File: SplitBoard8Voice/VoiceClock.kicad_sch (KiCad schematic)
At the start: 41 parts, among them U1001 74HC74, U1002 74HC595, U1003 74HC74, U1004 74HC08, U1005 74HC595, U1006 74HC14, U1007 74HC14

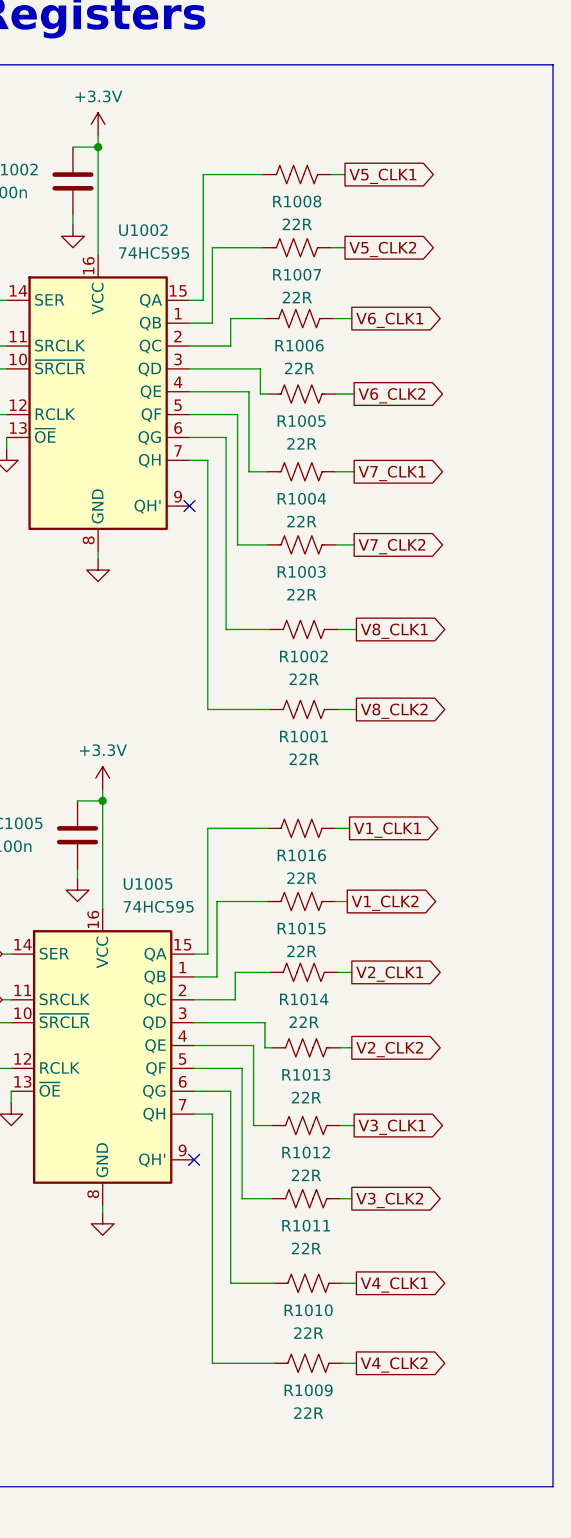
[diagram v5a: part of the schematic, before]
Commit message: some 8voice routing
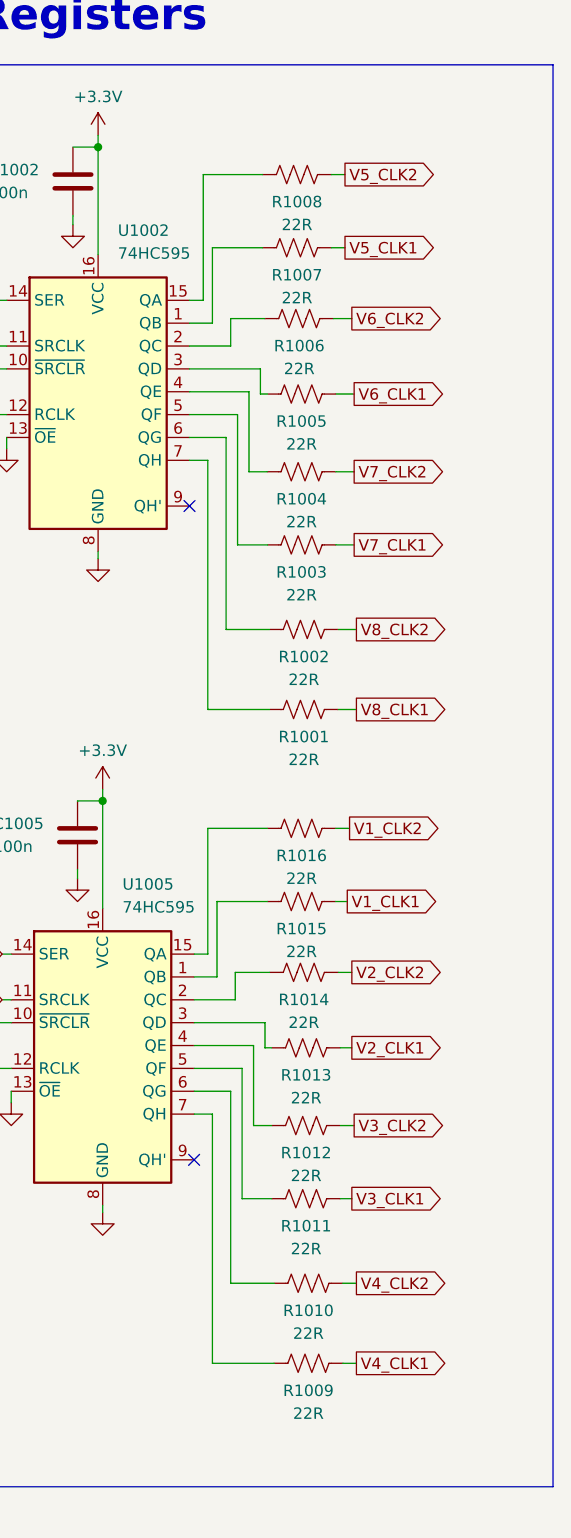
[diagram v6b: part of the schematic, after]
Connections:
- net V1_CLK1: now also R1015.2; no longer R1016.2
- net V1_CLK2: now also R1016.2; no longer R1015.2
- net V2_CLK1: now also R1013.2; no longer R1014.2
- net V2_CLK2: now also R1014.2; no longer R1013.2
- net V3_CLK1: now also R1011.2; no longer R1012.2
- net V3_CLK2: now also R1012.2; no longer R1011.2
- net V4_CLK1: now also R1009.2; no longer R1010.2
- net V4_CLK2: now also R1010.2; no longer R1009.2
- net V5_CLK1: now also R1007.2; no longer R1008.2
- net V5_CLK2: now also R1008.2; no longer R1007.2
- net V6_CLK1: now also R1005.2; no longer R1006.2
- net V6_CLK2: now also R1006.2; no longer R1005.2
- net V7_CLK1: now also R1003.2; no longer R1004.2
- net V7_CLK2: now also R1004.2; no longer R1003.2
- net V8_CLK1: now also R1001.2; no longer R1002.2
- net V8_CLK2: now also R1002.2; no longer R1001.2

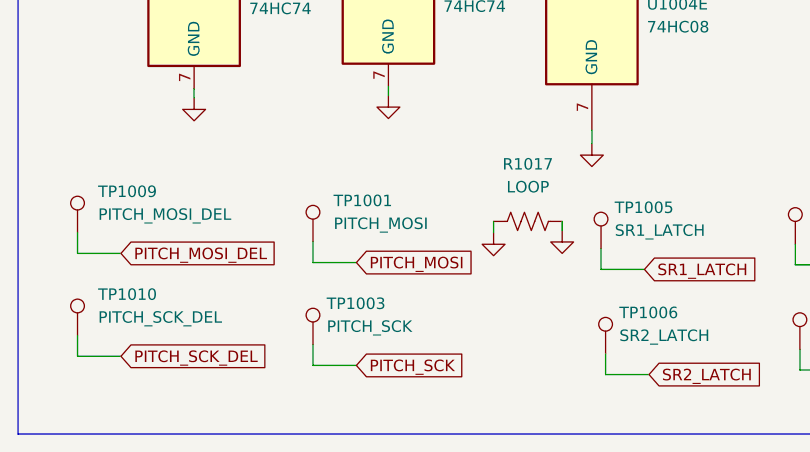
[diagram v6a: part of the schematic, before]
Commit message: transfer vias and test points added
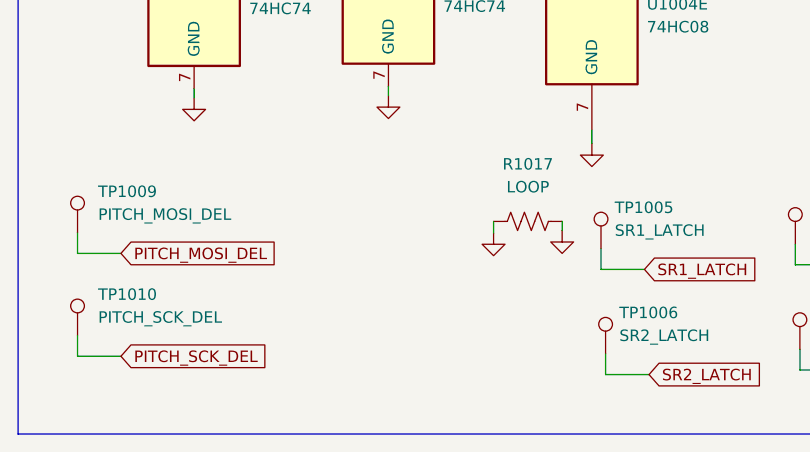
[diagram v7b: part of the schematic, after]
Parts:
- removed TP1001: PITCH_MOSI, TestPoint:TestPoint_THTPad_D1.0mm_Drill0.5mm_VAL, symbol Connector:TestPoint
- removed TP1003: PITCH_SCK, TestPoint:TestPoint_THTPad_D1.0mm_Drill0.5mm_VAL, symbol Connector:TestPoint
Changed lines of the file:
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@@
 	(wire
 		(pts
-			(xy 70.866 238.506) (xy 70.866 240.792)
-		)
-		(stroke
-			(width 0)
-			(type default)
-		)
-	)
-	(wire
-		(pts
 			(xy 336.55 46.99) (xy 338.074 46.99)
 		)
@@
 	(wire
 		(pts
-			(xy 70.866 240.792) (xy 75.692 240.792)
-		)
-		(stroke
-			(width 0)
-			(type default)
-		)
-	)
-	(wire
-		(pts
 			(xy 154.432 59.69) (xy 159.766 59.69)
 		)
@@
 	(wire
 		(pts
-			(xy 70.866 229.362) (xy 75.692 229.362)
-		)
-		(stroke
-			(width 0)
-			(type default)
-		)
-	)
-	(wire
-		(pts
 			(xy 298.958 73.66) (xy 300.482 73.66)
 		)
@@
 	(wire
 		(pts
-			(xy 70.866 227.076) (xy 70.866 229.362)
-		)
-		(stroke
-			(width 0)
-			(type default)
-		)
-	)
-	(wire
-		(pts
 			(xy 157.988 42.672) (xy 179.324 42.672)
 		)
@@
 		)
 	)
-	(global_label "PITCH_SCK"
-		(shape input)
-		(at 75.692 240.792 0)
-		(fields_autoplaced yes)
-		(effects
-			(font
-				(size 1.27 1.27)
-			)
-			(justify left)
-		)
-		(property "Intersheetrefs" "${INTERSHEET_REFS}"
-			(at 88.8372 240.792 0)
-			(effects
-				(font
-					(size 1.27 1.27)
-				)
-				(justify left)
-				(hide yes)
-			)
-		)
-	)
 	(global_label "V6_CLK2"
 		(shape output)
@@
 		)
 	)
-	(global_label "PITCH_MOSI"
-		(shape input)
-		(at 75.692 229.362 0)
-		(fields_autoplaced yes)
-		(effects
-			(font
-				(size 1.27 1.27)
-			)
-			(justify left)
-		)
-		(property "Intersheetrefs" "${INTERSHEET_REFS}"
-			(at 89.6839 229.362 0)
-			(effects
-				(font
-					(size 1.27 1.27)
-				)
-				(justify left)
-				(hide yes)
-			)
-		)
-	)
 	(symbol
 		(lib_id "Connector:TestPoint")
@@
 		(exclude_from_sim no)
 		(in_bom no)
-		(on_board no)
+		(on_board yes)
 		(dnp no)
 		(fields_autoplaced yes)
@@
 		(exclude_from_sim no)
 		(in_bom no)
-		(on_board no)
+		(on_board yes)
 		(dnp no)
 		(fields_autoplaced yes)
@@
 	)
 	(symbol
-		(lib_id "Connector:TestPoint")
-		(at 70.866 227.076 0)
-		(unit 1)
-		(exclude_from_sim no)
-		(in_bom no)
-		(on_board no)
-		(dnp no)
-		(fields_autoplaced yes)
-		(property "Reference" "TP1001"
-			(at 73.152 222.5039 0)
-			(effects
-				(font
-					(size 1.27 1.27)
-				)
-				(justify left)
-			)
-		)
-		(property "Value" "PITCH_MOSI"
-			(at 73.152 225.0439 0)
-			(effects
-				(font
-					(size 1.27 1.27)
-				)
-				(justify left)
-			)
-		)
-		(property "Footprint" "TestPoint:TestPoint_THTPad_D1.0mm_Drill0.5mm_VAL"
-			(at 75.946 227.076 0)
-			(effects
-				(font
-					(size 1.27 1.27)
-				)
-				(hide yes)
-			)
-		)
-		(property "Datasheet" "~"
-			(at 75.946 227.076 0)
-			(effects
-				(font
-					(size 1.27 1.27)
-				)
-				(hide yes)
-			)
-		)
-		(property "Description" "test point"
-			(at 70.866 227.076 0)
-			(effects
-				(font
-					(size 1.27 1.27)
-				)
-				(hide yes)
-			)
-		)
-		(pin "1"
-		)
-		(instances
-			(project "SplitBoard8Voice"
-				(path "/22649217-9810-470f-bc7b-6f743ad2b90e/3d9ecb3b-9556-42d6-955a-a32d9efd5d3a/c18fe030-c86d-45ba-9286-9b340d3ea677"
-					(reference "TP1001")
-					(unit 1)
-				)
-			)
-		)
-	)
-	(symbol
 		(lib_id "74xx:74HC14")
 		(at 202.946 185.674 0)
@@
 		(exclude_from_sim no)
 		(in_bom no)
-		(on_board no)
+		(on_board yes)
 		(dnp no)
 		(fields_autoplaced yes)
@@
 		(exclude_from_sim no)
 		(in_bom no)
-		(on_board no)
+		(on_board yes)
 		(dnp no)
 		(fields_autoplaced yes)
@@
 		(exclude_from_sim no)
 		(in_bom no)
-		(on_board no)
+		(on_board yes)
 		(dnp no)
 		(fields_autoplaced yes)
@@
 	)
 	(symbol
-		(lib_id "Connector:TestPoint")
-		(at 70.866 238.506 0)
-		(unit 1)
-		(exclude_from_sim no)
-		(in_bom no)
-		(on_board no)
-		(dnp no)
-		(fields_autoplaced yes)
-		(property "Reference" "TP1003"
-			(at 72.39 233.9339 0)
-			(effects
-				(font
-					(size 1.27 1.27)
-				)
-				(justify left)
-			)
-		)
-		(property "Value" "PITCH_SCK"
-			(at 72.39 236.4739 0)
-			(effects
-				(font
-					(size 1.27 1.27)
-				)
-				(justify left)
-			)
-		)
-		(property "Footprint" "TestPoint:TestPoint_THTPad_D1.0mm_Drill0.5mm_VAL"
-			(at 75.946 238.506 0)
-			(effects
-				(font
-					(size 1.27 1.27)
-				)
-				(hide yes)
-			)
-		)
-		(property "Datasheet" "~"
-			(at 75.946 238.506 0)
-			(effects
-				(font
-					(size 1.27 1.27)
-				)
-				(hide yes)
-			)
-		)
-		(property "Description" "test point"
-			(at 70.866 238.506 0)
-			(effects
-				(font
-					(size 1.27 1.27)
-				)
-				(hide yes)
-			)
-		)
-		(pin "1"
-		)
-		(instances
-			(project "SplitBoard8Voice"
-				(path "/22649217-9810-470f-bc7b-6f743ad2b90e/3d9ecb3b-9556-42d6-955a-a32d9efd5d3a/c18fe030-c86d-45ba-9286-9b340d3ea677"
-					(reference "TP1003")
-					(unit 1)
-				)
-			)
-		)
-	)
-	(symbol
 		(lib_id "74xx:74HC74")
 		(at 82.55 59.182 0)
@@
 		(exclude_from_sim no)
 		(in_bom no)
-		(on_board no)
+		(on_board yes)
 		(dnp no)
 		(fields_autoplaced yes)
@@
 		(exclude_from_sim no)
 		(in_bom no)
-		(on_board no)
+		(on_board yes)
 		(dnp no)
 		(fields_autoplaced yes)
@@
 		(exclude_from_sim no)
 		(in_bom no)
-		(on_board no)
+		(on_board yes)
 		(dnp no)
 		(fields_autoplaced yes)

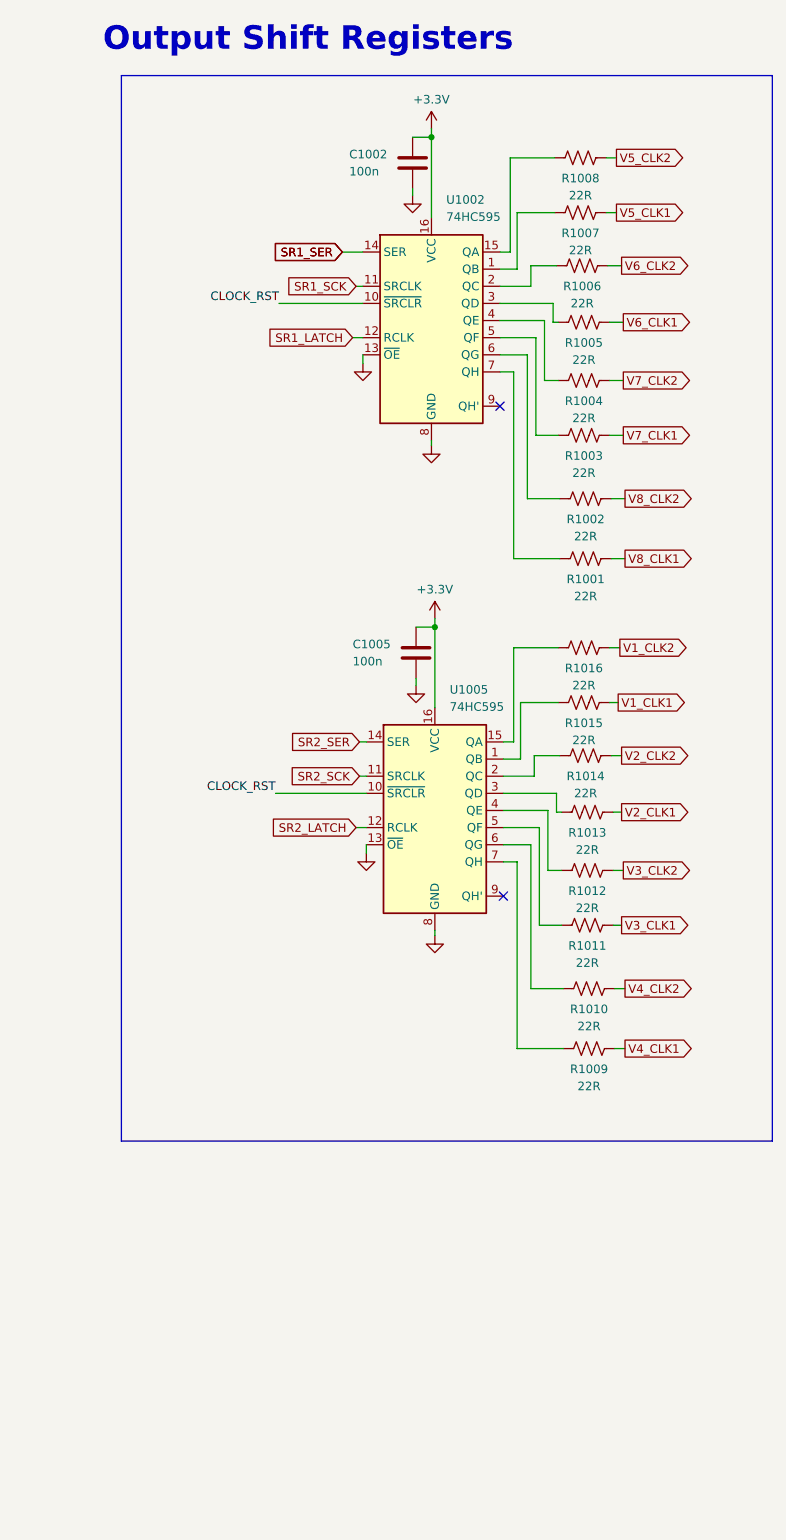
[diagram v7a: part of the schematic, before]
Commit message: silkscreen stuff, spacing cleanup
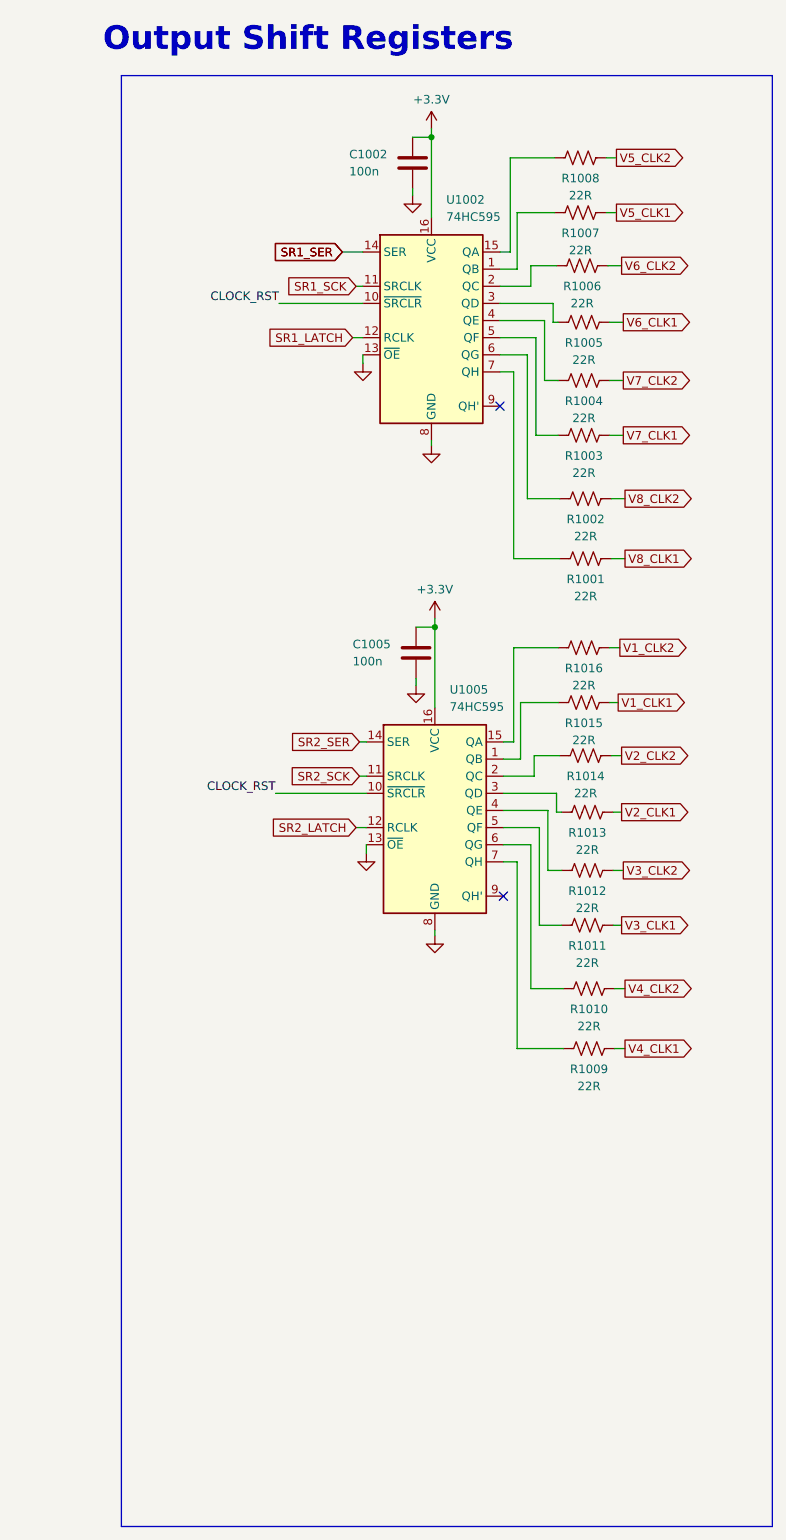
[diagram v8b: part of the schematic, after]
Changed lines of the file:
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@@
 	(rectangle
 		(start 264.668 34.798)
-		(end 361.188 192.786)
+		(end 361.188 249.936)
 		(stroke
 			(width 0)
